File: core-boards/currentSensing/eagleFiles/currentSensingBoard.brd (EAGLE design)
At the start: 52 x 64.6 mm, 23 parts, among them Q1 16MHz, X1 3-PIN_2MM-H, X2 2-PIN_2MM-H, X3 4-PIN_2MM-H

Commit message: Changes to Board Complete
-Most recent round of commentes taken account of
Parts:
- moved C3 1.00 mm to (5.80, 36.0)
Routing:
- net GND: track 29.2 -> 28.2 mm, vias 14 -> 13
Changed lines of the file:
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@@
 <elements>
 <element name="C1" library="rcl" library_urn="urn:adsk.eagle:library:334" package="C0603" package3d_urn="urn:adsk.eagle:package:23616/2" value="0.1 µF" x="4.65" y="39.03" smashed="yes" rot="R270">
-<attribute name="NAME" x="6.385" y="38.565" size="1" layer="25" font="vector"/>
+<attribute name="NAME" x="1.985" y="38.665" size="1" layer="25" font="vector"/>
 <attribute name="POPULARITY" value="37" x="4.65" y="39.03" size="1.778" layer="27" rot="R270" display="off"/>
 <attribute name="SPICEPREFIX" value="C" x="4.65" y="39.03" size="1.778" layer="27" rot="R270" display="off"/>
@@
 </element>
 <element name="C2" library="rcl" library_urn="urn:adsk.eagle:library:334" package="C0603" package3d_urn="urn:adsk.eagle:package:23616/2" value="0.1 µF" x="4.75" y="42.12" smashed="yes" rot="R90">
-<attribute name="NAME" x="7.215" y="45.215" size="1" layer="25" font="vector" rot="R180"/>
+<attribute name="NAME" x="3.215" y="42.215" size="1" layer="25" font="vector" rot="R180"/>
 <attribute name="POPULARITY" value="37" x="4.75" y="42.12" size="1.778" layer="27" rot="R90" display="off"/>
 <attribute name="SPICEPREFIX" value="C" x="4.75" y="42.12" size="1.778" layer="27" rot="R90" display="off"/>
 <attribute name="VALUE" x="6.655" y="41.485" size="1.27" layer="27" rot="R90"/>
 </element>
-<element name="C3" library="rcl" library_urn="urn:adsk.eagle:library:334" package="C0603" package3d_urn="urn:adsk.eagle:package:23616/2" value="0.1 µF" x="5.8" y="36.95" smashed="yes" rot="R180">
-<attribute name="NAME" x="8.635" y="35.915" size="1" layer="25" font="vector" rot="R180"/>
-<attribute name="POPULARITY" value="37" x="5.8" y="36.95" size="1.778" layer="27" rot="R180" display="off"/>
-<attribute name="SPICEPREFIX" value="C" x="5.8" y="36.95" size="1.778" layer="27" rot="R180" display="off"/>
-<attribute name="VALUE" x="6.435" y="38.855" size="1.27" layer="27" rot="R180"/>
+<element name="C3" library="rcl" library_urn="urn:adsk.eagle:library:334" package="C0603" package3d_urn="urn:adsk.eagle:package:23616/2" value="0.1 µF" x="5.8" y="35.95" smashed="yes" rot="R180">
+<attribute name="NAME" x="3.635" y="33.915" size="1" layer="25" font="vector" rot="R180"/>
+<attribute name="POPULARITY" value="37" x="5.8" y="35.95" size="1.778" layer="27" rot="R180" display="off"/>
+<attribute name="SPICEPREFIX" value="C" x="5.8" y="35.95" size="1.778" layer="27" rot="R180" display="off"/>
+<attribute name="VALUE" x="6.435" y="37.855" size="1.27" layer="27" rot="R180"/>
 </element>
 <element name="C4" library="rcl" library_urn="urn:adsk.eagle:library:334" package="C0603" package3d_urn="urn:adsk.eagle:package:23616/2" value="0.1 µF" x="19.55" y="39.88" smashed="yes" rot="R90">
@@
 <wire x1="4.18" y1="38.18" x2="3" y2="37" width="0.3048" layer="1"/>
 <via x="3" y="37" extent="1-16" drill="0.35"/>
-<wire x1="4.95" y1="36.95" x2="6" y2="35.9" width="0.3048" layer="1"/>
-<wire x1="6" y1="35.9" x2="6" y2="34" width="0.3048" layer="1"/>
+<wire x1="4.95" y1="35.95" x2="6" y2="34.9" width="0.3048" layer="1"/>
+<wire x1="6" y1="34.9" x2="6" y2="34" width="0.3048" layer="1"/>
 <via x="6" y="34" extent="1-16" drill="0.35"/>
-<via x="4" y="24" extent="1-16" drill="0.35"/>
 <wire x1="20.4" y1="19.85" x2="18.75" y2="19.85" width="0.3048" layer="1"/>
 <wire x1="18.75" y1="19.85" x2="18.3" y2="19.4" width="0.3048" layer="1"/>
@@
 <wire x1="17.88" y1="38.12" x2="18" y2="38" width="0.3048" layer="1"/>
 <via x="18" y="38" extent="1-16" drill="0.35"/>
-<wire x1="18" y1="38" x2="22" y2="38" width="0.3048" layer="16"/>
-<wire x1="22" y1="38" x2="25" y2="41" width="0.3048" layer="16"/>
+<wire x1="18" y1="38" x2="19" y2="39" width="0.3048" layer="16"/>
+<wire x1="23" y1="39" x2="19" y2="39" width="0.3048" layer="16"/>
+<wire x1="23" y1="39" x2="25" y2="41" width="0.3048" layer="16"/>
 <via x="25" y="41" extent="1-16" drill="0.35"/>
 <wire x1="25" y1="41" x2="26" y2="42" width="0.3048" layer="1"/>

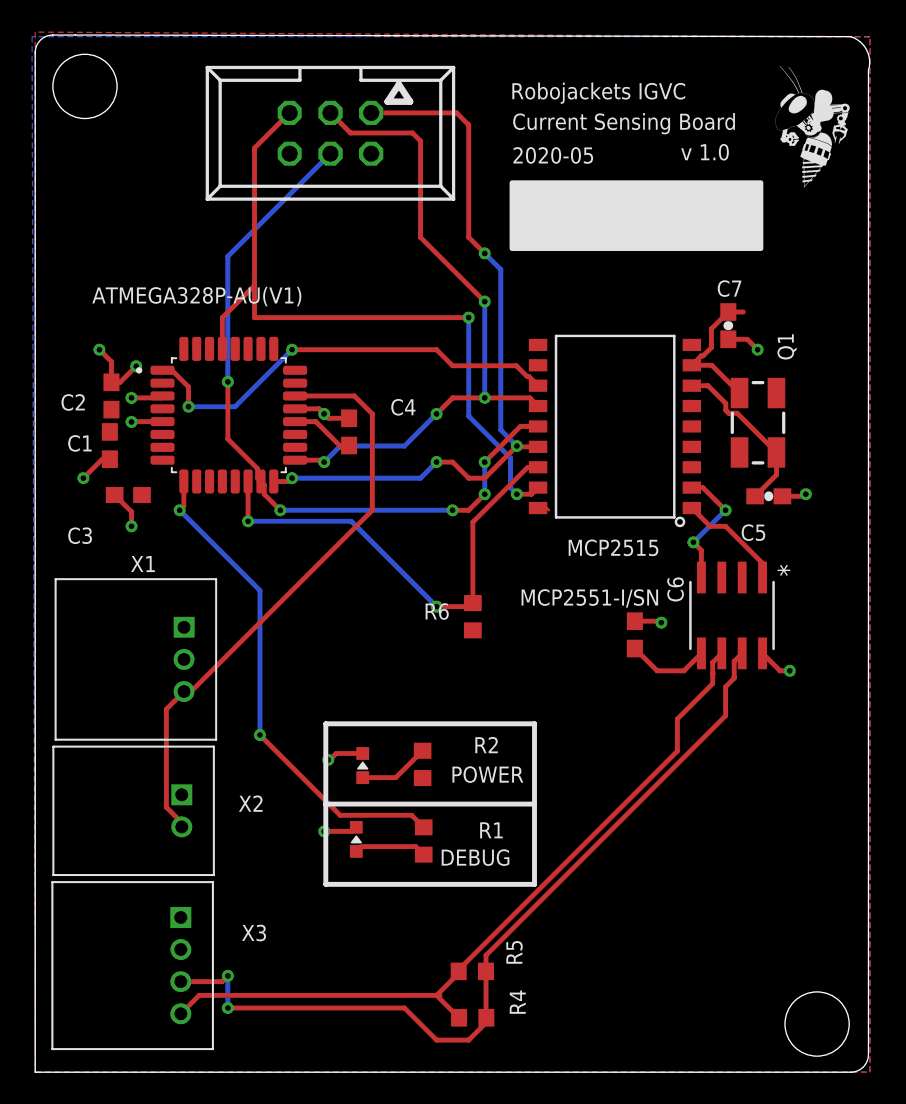
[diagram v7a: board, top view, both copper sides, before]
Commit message: Airwires/stubs fixed
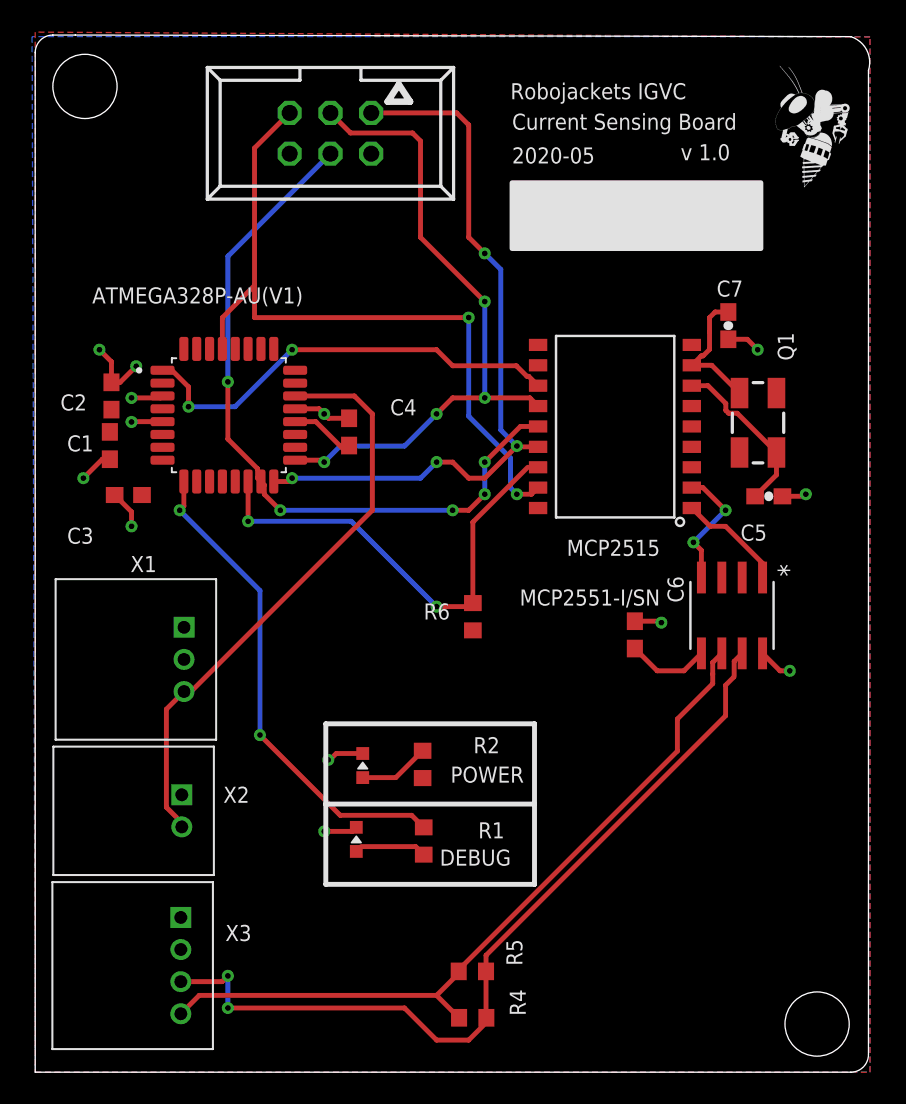
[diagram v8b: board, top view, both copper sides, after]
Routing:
- net VDD: track 0.74 -> 0.00 mm
- net N$17: track 9.16 -> 8.50 mm
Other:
- board text added: "!RS"
- board text added: "MISO"
- board text added: "SCK"
- board text added: "Sensor Output"
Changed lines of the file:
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@@
 <wire x1="18.1" y1="16.7" x2="31.1" y2="16.7" width="0.3048" layer="21"/>
 <wire x1="31.1" y1="16.7" x2="31.1" y2="21.7" width="0.3048" layer="21"/>
-<text x="13" y="6" size="0.9" layer="51" font="vector">CAN_P</text>
-<text x="13" y="2" size="0.9" layer="51" font="vector">CAN_N</text>
+<text x="13" y="6" size="0.5" layer="51" font="vector">CAN_P</text>
+<text x="13" y="3" size="0.5" layer="51" font="vector">CAN_N</text>
 <wire x1="18.1" y1="11.7" x2="31.1" y2="11.7" width="0.3048" layer="21"/>
 <wire x1="18.1" y1="16.7" x2="18.1" y2="11.7" width="0.3048" layer="21"/>
 <wire x1="31.1" y1="16.7" x2="31.1" y2="11.7" width="0.3048" layer="21"/>
 <text x="4" y="58" size="1" layer="51">4mm</text>
+<text x="12" y="15" size="0.5" layer="51" font="vector">Sensor Output</text>
+<text x="12" y="23" size="0.5" layer="51" font="vector">Sensor Output</text>
+<text x="15" y="63" size="0.5" layer="51" font="vector">!RS</text>
+<text x="18" y="63" size="0.5" layer="51" font="vector">SCK</text>
+<text x="21" y="63" size="0.5" layer="51" font="vector">MISO</text>
 </plain>
 <attributes>
@@
 <attribute name="DIGIKEY" value="WM18933-ND" x="9.07" y="6.64" size="1.778" layer="27" rot="R270" display="off"/>
 <attribute name="MPN" value="0353630460" x="9.07" y="6.64" size="1.778" layer="27" rot="R270" display="off"/>
-<attribute name="NAME" x="13.66" y="8.17" size="1" layer="25" font="vector" ratio="10" align="bottom-center"/>
+<attribute name="NAME" x="12.66" y="8.17" size="1" layer="25" font="vector" ratio="10" align="bottom-center"/>
 </element>
 <element name="X1" library="RoboJackets-Connectors" package="2MM-3-H" value="3-PIN_2MM-H" x="9.27" y="25.71" smashed="yes" rot="R270">
@@
 </element>
 <element name="X2" library="RoboJackets-Connectors" package="2MM-2-H" value="2-PIN_2MM-H" x="9.13" y="17.28" smashed="yes" rot="R270">
-<attribute name="NAME" x="13.47" y="16.22" size="1" layer="25" font="vector" ratio="10" align="bottom-center"/>
+<attribute name="NAME" x="12.53" y="17.78" size="1" layer="25" font="vector" ratio="10" rot="R180" align="bottom-center"/>
 <attribute name="PINS" value="2" x="9.13" y="17.28" size="1.778" layer="27" rot="R270" display="off"/>
 <attribute name="PIN_PITCH" value="2.0 mm" x="9.13" y="17.28" size="1.778" layer="27" rot="R270" display="off"/>
@@
 <signal name="VDD">
 <contactref element="MCP2515" pad="18"/>
-<wire x1="31.3221" y1="35.14" x2="31.86" y2="35.14" width="0.1524" layer="1"/>
-<wire x1="31.86" y1="35.14" x2="32" y2="35" width="0.1524" layer="1"/>
 </signal>
 <signal name="VSS">
@@
 <wire x1="43.535" y1="25.5878" x2="43.535" y2="24.635" width="0.3048" layer="1"/>
 <wire x1="43.535" y1="25.5878" x2="44.035" y2="26.0878" width="0.3048" layer="1"/>
-<wire x1="43" y1="24" x2="43.535" y2="24.535" width="0.3048" layer="1"/>
-<wire x1="43.535" y1="24.535" x2="43.535" y2="24.635" width="0.3048" layer="1"/>
-<wire x1="12.105" y1="3.895" x2="12" y2="4" width="0.3048" layer="1"/>
 <via x="12" y="4" extent="1-16" drill="0.35"/>
 <wire x1="12" y1="4" x2="12" y2="6" width="0.3048" layer="16"/>
@@
 <wire x1="11.64" y1="5.64" x2="9.07" y2="5.64" width="0.3048" layer="1"/>
 <wire x1="28.08" y1="6.28" x2="28.08" y2="7.28" width="0.3048" layer="1"/>
-<wire x1="43" y1="22.2" x2="43" y2="24" width="0.3048" layer="1"/>
 <wire x1="28.08" y1="7.28" x2="43" y2="22.2" width="0.3048" layer="1"/>
 <wire x1="28.08" y1="6.28" x2="28.08" y2="3.41" width="0.3048" layer="1"/>
@@
 <wire x1="27" y1="2" x2="28.08" y2="3.08" width="0.3048" layer="1"/>
 <wire x1="28.08" y1="3.08" x2="28.08" y2="3.41" width="0.3048" layer="1"/>
+<wire x1="43" y1="24.1" x2="43.5" y2="24.6" width="0.3048" layer="1"/>
+<wire x1="43" y1="22.2" x2="43" y2="24.1" width="0.3048" layer="1"/>
 </signal>
 <signal name="CAN_N">
@@
 <contactref element="R4" pad="1"/>
 <contactref element="R5" pad="1"/>
-<wire x1="42.22566875" y1="24.82566875" x2="42.2" y2="24.8" width="0.3048" layer="1"/>
 <wire x1="42.2" y1="24.8" x2="42.2" y2="25.5228" width="0.3048" layer="1"/>
 <wire x1="42.2" y1="25.5228" x2="42.765" y2="26.0878" width="0.3048" layer="1"/>
 <wire x1="10.215" y1="4.785" x2="9.07" y2="3.64" width="0.3048" layer="1"/>
 <wire x1="10.215" y1="4.785" x2="25" y2="4.785" width="0.3048" layer="1"/>
-<wire x1="25.215" y1="4.785" x2="25" y2="4.785" width="0.3048" layer="1"/>
 <wire x1="42.2" y1="24.2" x2="42.2" y2="24.8" width="0.3048" layer="1"/>
 <wire x1="40" y1="22" x2="40" y2="20" width="0.3048" layer="1"/>
@@
 <contactref element="MCP2551-I/SN" pad="1"/>
 <contactref element="MCP2515" pad="1"/>
-<wire x1="45.305" y1="30.8122" x2="45.1878" y2="30.8122" width="0.3048" layer="1"/>
 <wire x1="40.8979" y1="35.14" x2="42.0379" y2="34" width="0.3048" layer="1"/>
 <wire x1="42.0379" y1="34" x2="43" y2="34" width="0.3048" layer="1"/>
@@
 <contactref element="X1" pad="3"/>
 <contactref element="X2" pad="2"/>
-<wire x1="9.13" y1="15.28" x2="9.0888" y2="15.3212" width="0.3048" layer="1"/>
 <wire x1="9.13" y1="15.28" x2="9.13" y2="15.54095" width="0.3048" layer="1"/>
 <wire x1="9.13" y1="15.54095" x2="8.1712" y2="16.49975" width="0.3048" layer="1"/>
@@
 <contactref element="C7" pad="2"/>
 <contactref element="MCP2515" pad="8"/>
-<wire x1="43.17" y1="47.35" x2="44.100646875" y2="47.35" width="0.3048" layer="1"/>
-<wire x1="43.17" y1="47.35" x2="43.02" y2="47.2" width="0.3048" layer="1"/>
 <wire x1="41.4821" y1="44.6142" x2="41.59565" y2="44.6142" width="0.3048" layer="1"/>
 <wire x1="41.4821" y1="44.6142" x2="40.8979" y2="44.03" width="0.3048" layer="1"/>
-<wire x1="42.12" y1="46.3" x2="43.17" y2="47.35" width="0.3048" layer="1"/>
-<wire x1="42.12" y1="45.13855" x2="42.12" y2="46.3" width="0.3048" layer="1"/>
-<wire x1="41.59565" y1="44.6142" x2="42.12" y2="45.13855" width="0.3048" layer="1"/>
+<wire x1="42" y1="45.01855" x2="42" y2="46.12" width="0.3048" layer="1"/>
+<wire x1="41.59565" y1="44.6142" x2="42" y2="45.01855" width="0.3048" layer="1"/>
 <wire x1="40.8979" y1="44.03" x2="42.14" y2="44.03" width="0.3048" layer="1"/>
 <wire x1="42.14" y1="44.03" x2="43.87" y2="42.3" width="0.3048" layer="1"/>
+<wire x1="42" y1="46.12" x2="42" y2="47" width="0.3048" layer="1"/>
+<wire x1="42" y1="47" x2="42.35" y2="47.35" width="0.3048" layer="1"/>
+<wire x1="42.35" y1="47.35" x2="43.17" y2="47.35" width="0.3048" layer="1"/>
 </signal>
 <signal name="N$18">
